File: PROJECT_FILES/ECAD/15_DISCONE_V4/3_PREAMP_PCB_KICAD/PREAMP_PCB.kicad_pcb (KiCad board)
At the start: 2 copper layers, 51 x 25 mm, 22 parts

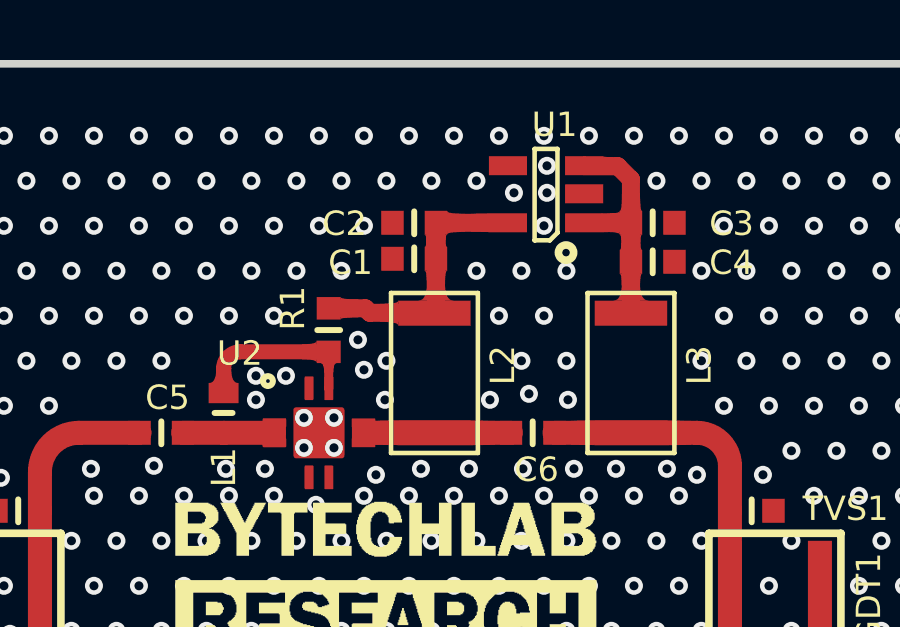
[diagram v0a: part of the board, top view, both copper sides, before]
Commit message: Update jobset & exported files
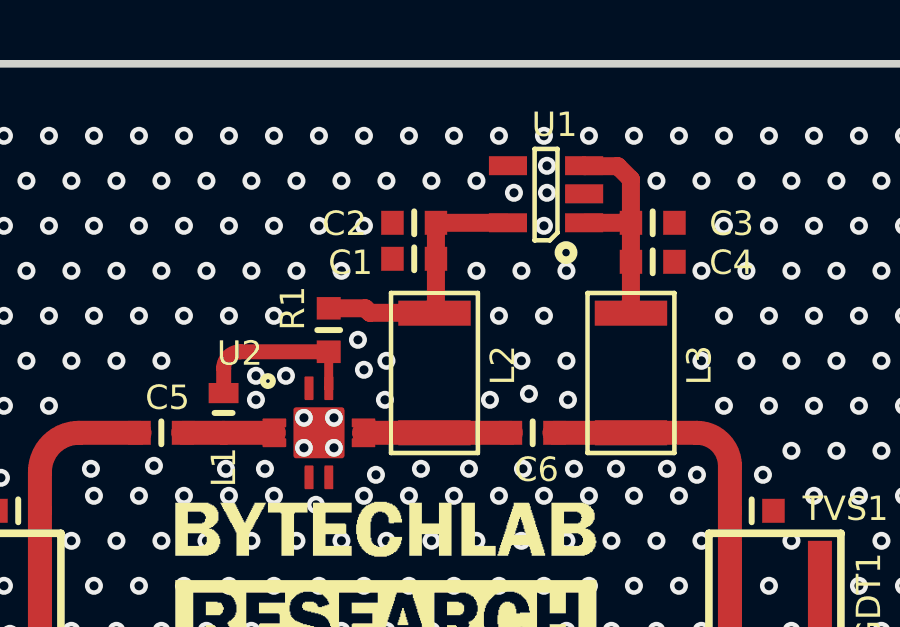
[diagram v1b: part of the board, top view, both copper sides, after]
